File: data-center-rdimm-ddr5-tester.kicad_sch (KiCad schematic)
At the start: 2 parts

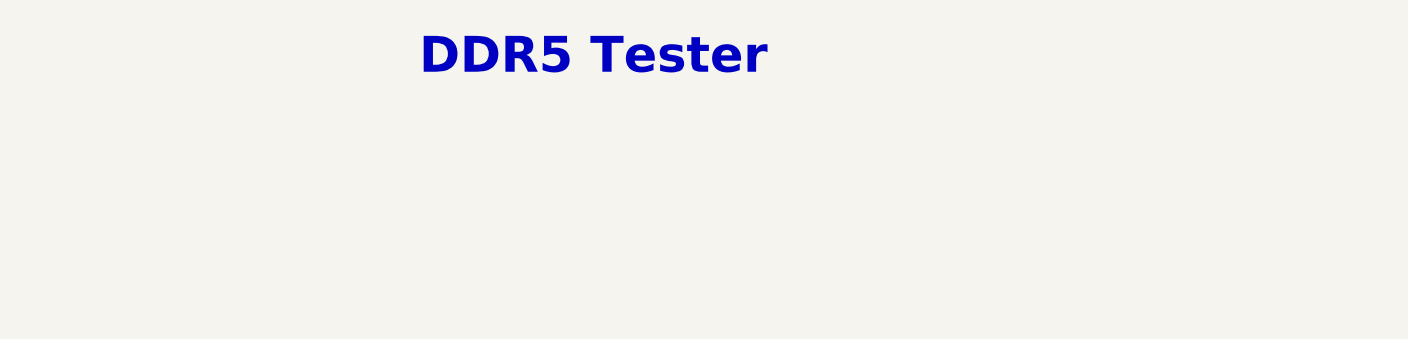
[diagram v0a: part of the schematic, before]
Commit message: Update naming on the front page
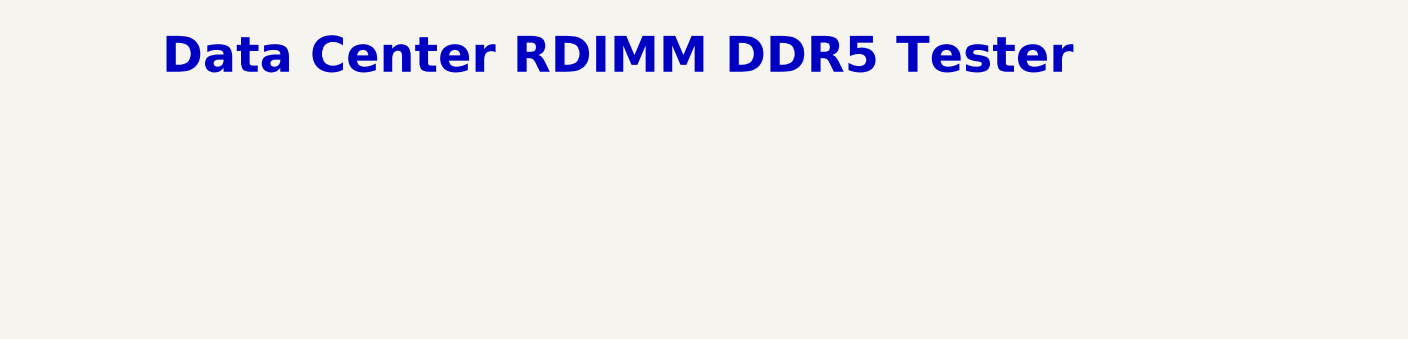
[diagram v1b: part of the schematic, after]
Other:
- note added: "Data Center RDIMM DDR5 Tester"
- note removed: "DDR5 Tester"
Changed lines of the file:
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@@
     )
   )
-  (text "DDR5 Tester" (at 193.04 36.195 0)
+  (text "Data Center RDIMM DDR5 Tester" (at 164.465 36.195 0)
     (effects (font (size 3.9878 3.9878) (thickness 0.7976) bold) (justify left bottom))
   )

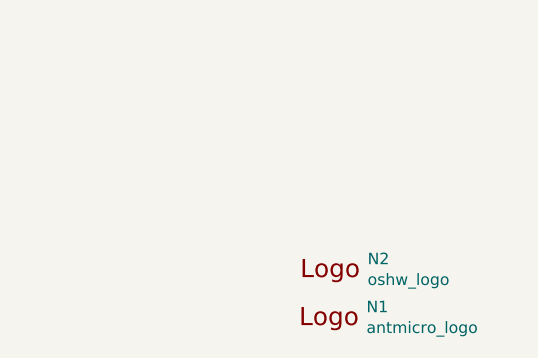
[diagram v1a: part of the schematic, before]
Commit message: Introduce component standarization
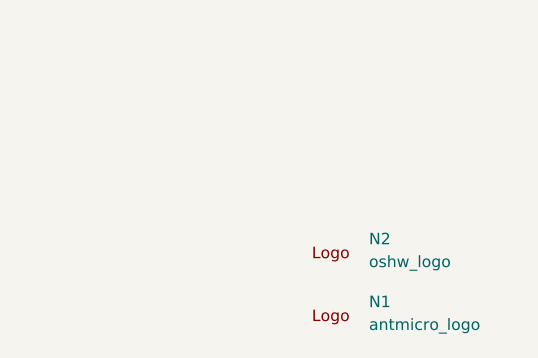
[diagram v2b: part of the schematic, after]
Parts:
- N1, N2: Author (none) -> Antmicro; License (none) -> Apache-2.0
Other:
- moved on the sheet: N1, N2

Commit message: [#55296] component update
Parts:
- N1: footprint data-center-rdimm-ddr5-tester-footprints:antmicro-logo_scaled_20mm -> data-center-rdimm-ddr5-tester-footprints:antmicro-logo
